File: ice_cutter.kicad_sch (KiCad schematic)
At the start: 156 parts, among them J1 Conn_01x01_Male, J2 Barrel_Jack, J3 pot, J4 Conn_01x01_Male, J5 program, J6 program2, J7 hands, J8 UART, J9 xt60, M1 Motor_Servo, M2 Motor_Servo, Q1 Q_PMOS_GSD, Q11 Q_NMOS_GSD, Q12 Q_NMOS_GSD, Q13 Q_NMOS_GSD, Q14 Q_NMOS_GSD, Q2 Q_PMOS_GSD, Q3 Q_PMOS_GSD, Q4 S8550, Q5 Q_NMOS_GSD, Q7 Q_NMOS_GSD, SW1 SW_Push, SW2 SW_Push, SW3 SW_Push, U1 LM317_TO-252, U10 TMP117, U11 TM1620, U12 INA219AxD, U2 LM317_TO-252, U3 INA219AxD, U4 LM317_TO-252, U5 INA219AxD, U6 FJ4301AH, U7 FJ4301AH, U8 STM32G030XX, U9 SHT30-DIS

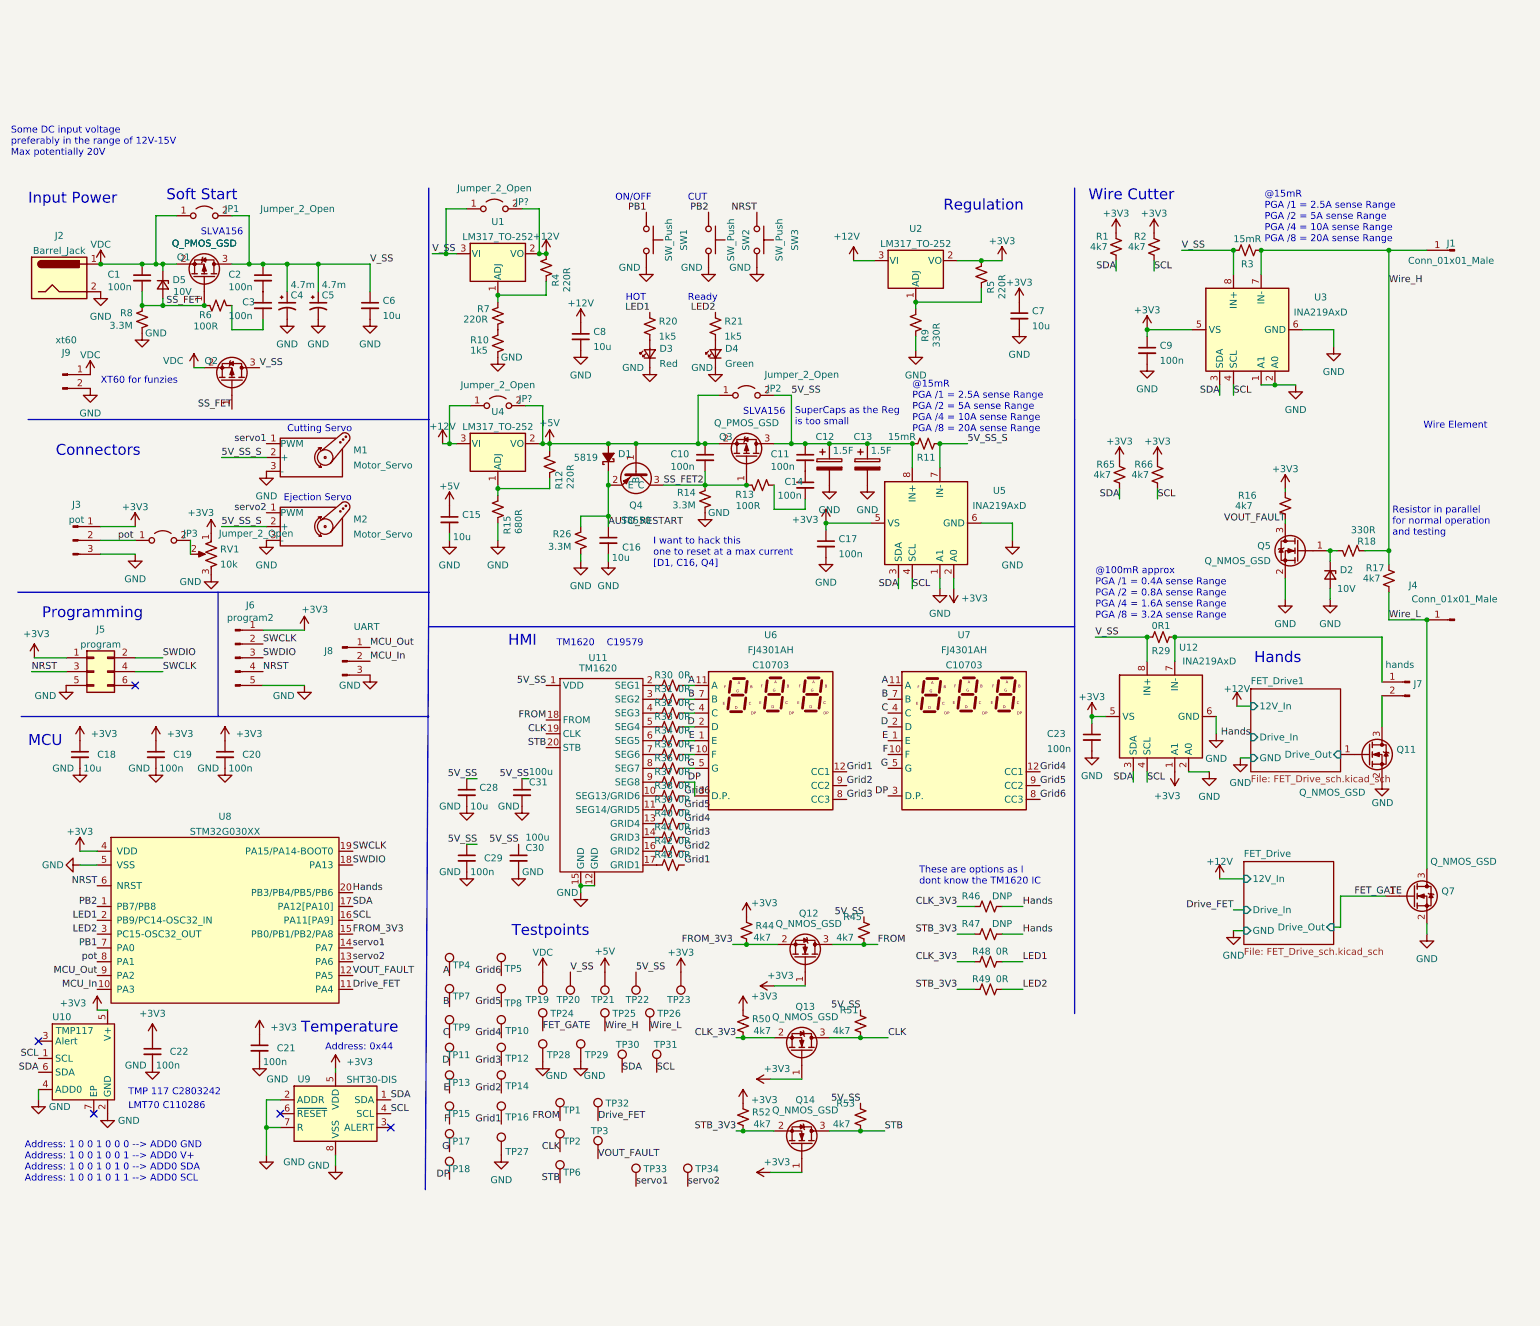
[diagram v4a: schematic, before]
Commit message: major schematic changes, 5V is now the highest voltage, added more FETs for Wire conduction, more for SS, opamp for current hack, removed Regs, XT60 and significantly changed wiring and R values for sections... Still a lot to be done, cant be solved now
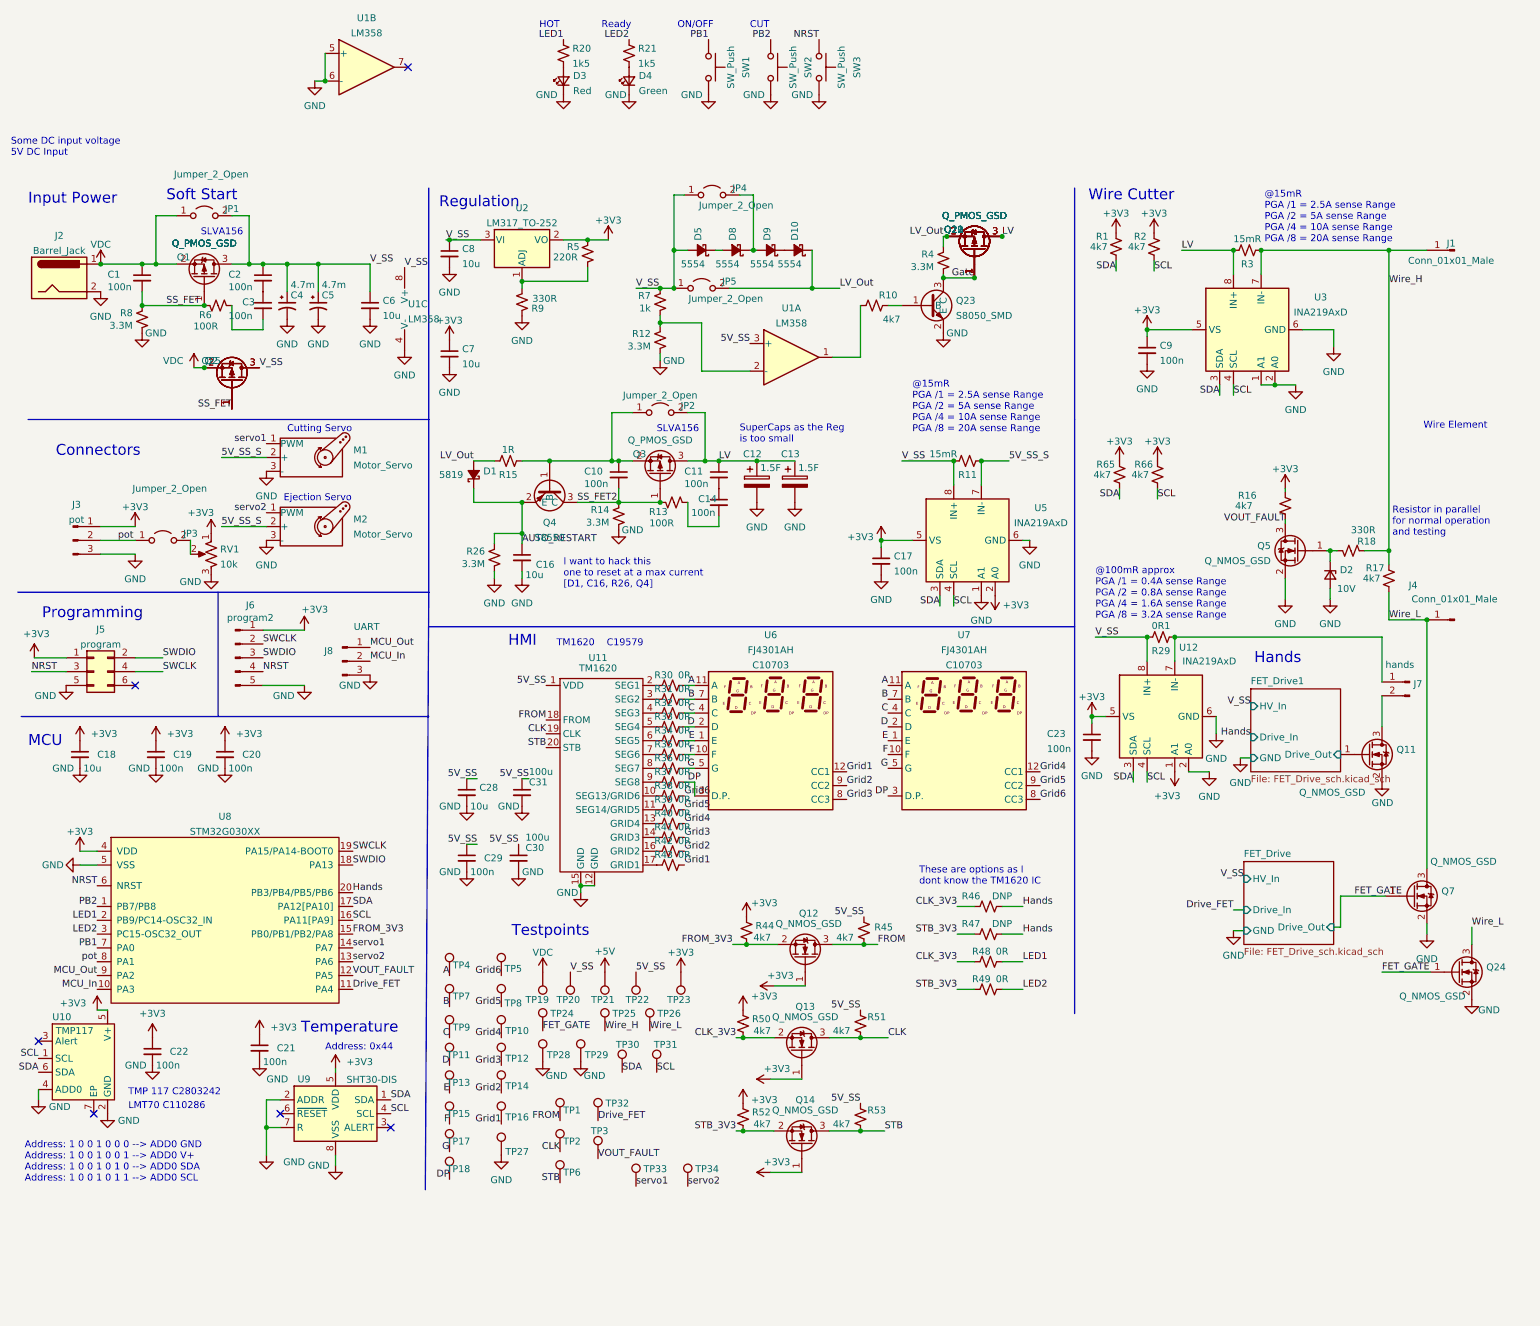
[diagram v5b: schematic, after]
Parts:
- removed C15: 10u, Capacitor_SMD:C_0603_1608Metric, symbol Device:C_Small
- removed D5: 10V, Diode_SMD:D_SOD-123, symbol Device:D_Zener_Small
- removed J9: xt60, UCT:XT60PW-M, symbol Connector:Conn_01x02_Male
- removed JP? (x2): Jumper_2_Open, Jumper:SolderJumper-2_P1.3mm_Open_RoundedPad1.0x1.5mm, symbol Jumper:Jumper_2_Open
- removed U1, U4: LM317_TO-252, Package_TO_SOT_SMD:TO-252-2, symbol Regulator_Linear:LM317_TO-252
- added D10, D5, D8, D9: 5554, Diode_SMD:D_SMA, symbol Device:D_Schottky_Small_Filled
- added JP4, JP5: Jumper_2_Open, Jumper:SolderJumper-2_P1.3mm_Open_RoundedPad1.0x1.5mm, symbol Jumper:Jumper_2_Open
- added Q19, Q20, Q21, Q22, Q25: Q_PMOS_GSD, Package_TO_SOT_SMD:SOT-23, symbol Device:Q_PMOS_GSD
- added Q23: S8050_SMD, Package_TO_SOT_SMD:SOT-23, symbol MyDevices:S8050_SMD
- added Q24: Q_NMOS_GSD, Package_TO_SOT_SMD:TO-252-2, symbol Device:Q_NMOS_GSD
- added U1: LM358, Package_SO:SOIC-8_3.9x4.9mm_P1.27mm, symbol Amplifier_Operational:LM358
- Q11, Q7: LCSC C130980 -> C709962
- R10: value 1k5 -> 4k7; LCSC C25867 -> C25900
- R12, R4: value 220R -> 3.3M; LCSC C25091 -> C25741
- R15: value 680R -> 1R; footprint Resistor_SMD:R_0402_1005Metric -> Resistor_SMD:R_2512_6332Metric; Extended 0 -> 1; LCSC C25130 -> C11254; Price 0.0007 -> 0.087
- R7: value 220R -> 1k; LCSC C25091 -> (none)
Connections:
- net +5V: no longer C10.1, D1.2 (A), JP2.1 (A), Q3.2 (S), Q4.1 (B), R12.2
- net 5V_SS: now also U1.3 (+); no longer C11.1, C12.1, C13.1, JP2.2 (B), Q3.3 (D), R11.1, U5.8 (IN+)
- net FET_GATE: now also Q24.1 (G)
- net GND: now also R12.2, Q23.2 (E), Q24.2 (S), U1.4 (V-), U1.5 (+), U1.6 (-); no longer R10.1, R15.1
- net SS_FET: now also Q25.1 (G)
- net VDC: now also Q25.2 (S)
- net V_SS: now also C8.1, R11.1, R7.1, U2.3 (VI), U5.8 (IN+), D5.2 (A), JP4.1 (A), JP5.1 (A), Q25.3 (D), U1.8 (V+); no longer R3.1, U3.8 (IN+)
- net Wire_L: now also Q24.3 (D)
- net at R7.2: now also R12.1, U1.2 (-); no longer R4.1
- net at R15.2: now also C10.1, JP2.1 (A), Q3.2 (S), Q4.1 (B); no longer R12.1
- net at R10.2: now also U1.1; no longer R7.1
- removed net +12V: C8.1, R4.2, U2.3 (VI)
- new net: D10.2 (A), D9.1 (K)
- new net: D8.1 (K), D9.2 (A), JP4.2 (B)
- new net: D5.1 (K), D8.2 (A)
- new net: Q23.1 (B), R10.1
- new net Gate: Q19.1 (G), Q20.1 (G), Q21.1 (G), Q22.1 (G), Q23.3 (C), R4.2
- new net LV: C11.1, C12.1, C13.1, JP2.2 (B), Q19.3 (D), Q20.3 (D), Q21.3 (D), Q22.3 (D), Q3.3 (D), R3.1, U3.8 (IN+)
- new net LV_Out: D1.2 (A), D10.1 (K), JP5.2 (B), Q19.2 (S), Q20.2 (S), Q21.2 (S), Q22.2 (S), R15.1, R4.1
- no-connect marks 5 -> 6
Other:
- sheet FET_Drive ports: added HV_In; removed 12V_In
- sheet FET_Drive1 ports: added HV_In; removed 12V_In
- note added: "I want to hack this one to reset at a max current [D1, C16, R26, Q4]"
- note added: "Some DC input voltage 5V DC Input"
- note removed: "I want to hack this one to reset at a max current [D1, C16, Q4]"
- note removed: "Some DC input voltage preferably in the range of 12V-15V Max potentially 20V"
- note removed: "XT60 for funzies"
- moved on the sheet: C10, C11, C12, C13, C14, C16, C17, C7, C8, D1, D3, D4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

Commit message: more mods, taking it to a solution. Mostly on layer 3 and power management
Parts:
- added C15: 100n, Capacitor_SMD:C_0402_1005Metric, symbol Device:C_Small
- R12: value 3.3M -> 4k7; LCSC C25741 -> C25900
- R7: value 1k -> 220R; LCSC (none) -> C25091
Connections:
- net 5V_SS: no longer C28.1, C29.1, C30.1, C31.1, R45.2, R51.2, R53.2, U11.1 (VDD)
- net GND: now also R12.1, C15.2; no longer R12.2
- net LV_Out: now also R7.2
- net V_SS: now also C28.1, C29.1, C30.1, C31.1, R45.2, R51.2, R53.2, U11.1 (VDD), C15.1; no longer R7.1
- new net: R12.2, R7.1, U1.2 (-)
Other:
- moved on the sheet: C28, C29, C30, C31, U1A

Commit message: potential new version. Still to do Silkscreen and resistor value confirmations
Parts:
- removed TP22: TestPoint, TestPoint:TestPoint_Pad_D2.0mm, symbol Connector:TestPoint
- added TP?: TestPoint, TestPoint:TestPoint_Pad_D2.0mm, symbol Connector:TestPoint
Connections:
- net 5V_SS is gone; now on net V_SS: U1.3 (+)
- net LV: now also TP?.1
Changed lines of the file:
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@@
     (effects (font (size 1.27 1.27)) (justify left bottom))
   )
+  (label "LV" (at 127 157.48 0)
+    (effects (font (size 1.27 1.27)) (justify left bottom))
+  )
   (label "MCU_In" (at 26.67 160.655 180)
     (effects (font (size 1.27 1.27)) (justify right bottom))
@@
     (effects (font (size 1.27 1.27)) (justify left bottom))
   )
+  (label "V_SS" (at 151.765 41.91 180)
+    (effects (font (size 1.27 1.27)) (justify right bottom))
+  )
   (label "NRST" (at 14.605 102.235 0)
     (effects (font (size 1.27 1.27)) (justify left bottom))
@@
     (effects (font (size 1.27 1.27)) (justify left bottom))
   )
-  (label "5V_SS" (at 125.73 157.48 0)
-    (effects (font (size 1.27 1.27)) (justify left bottom))
-  )
   (label "SWCLK" (at 73.66 135.255 0)
     (effects (font (size 1.27 1.27)) (justify left bottom))
@@
     (effects (font (size 1.27 1.27)) (justify left bottom))
   )
-  (label "5V_SS" (at 151.765 41.91 180)
-    (effects (font (size 1.27 1.27)) (justify right bottom))
-  )
   (label "Drive_FET" (at 73.66 160.655 0)
     (effects (font (size 1.27 1.27)) (justify left bottom))
@@
     (pin "1")
   )
-  (symbol (lib_id "Connector:TestPoint") (at 125.73 157.48 180) (unit 1)
-    (in_bom yes) (on_board yes)
-    (property "Reference" "TP22" (id 0) (at 123.825 162.56 0)
-      (effects (font (size 1.27 1.27)) (justify right))
-    )
-    (property "Value" "TestPoint" (id 1) (at 124.46 163.195 0)
-      (effects (font (size 1.27 1.27)) (justify right) hide)
-    )
-    (property "Footprint" "TestPoint:TestPoint_Pad_D2.0mm" (id 2) (at 120.65 157.48 0)
-      (effects (font (size 1.27 1.27)) hide)
-    )
-    (property "Datasheet" "~" (id 3) (at 120.65 157.48 0)
-      (effects (font (size 1.27 1.27)) hide)
-    )
-    (property "Populate" "No" (id 4) (at 125.73 157.48 0)
-      (effects (font (size 1.27 1.27)) hide)
-    )
-    (pin "1")
-  )
   (symbol (lib_id "Connector:Conn_01x03_Male") (at 22.225 78.105 0) (unit 1)
     (in_bom yes) (on_board yes) (fields_autoplaced)
@@
     (pin "3")
   )
+  (symbol (lib_id "Connector:TestPoint") (at 127 157.48 180) (unit 1)
+    (in_bom yes) (on_board yes)
+    (property "Reference" "TP?" (id 0) (at 124.46 162.56 0)
+      (effects (font (size 1.27 1.27)) (justify right))
+    )
+    (property "Value" "TestPoint" (id 1) (at 125.73 163.195 0)
+      (effects (font (size 1.27 1.27)) (justify right) hide)
+    )
+    (property "Footprint" "TestPoint:TestPoint_Pad_D2.0mm" (id 2) (at 121.92 157.48 0)
+      (effects (font (size 1.27 1.27)) hide)
+    )
+    (property "Datasheet" "~" (id 3) (at 121.92 157.48 0)
+      (effects (font (size 1.27 1.27)) hide)
+    )
+    (property "Populate" "No" (id 4) (at 127 157.48 0)
+      (effects (font (size 1.27 1.27)) hide)
+    )
+    (pin "1")
+  )
   (symbol (lib_id "power:GND") (at 36.83 174.625 0) (unit 1)
     (in_bom yes) (on_board yes)
@@
       (reference "TP21") (unit 1) (value "TestPoint") (footprint "TestPoint:TestPoint_Pad_D2.0mm")
     )
-    (path "/5cd2c641-9219-4ecf-8a99-e9ad548e97f6"
-      (reference "TP22") (unit 1) (value "TestPoint") (footprint "TestPoint:TestPoint_Pad_D2.0mm")
-    )
     (path "/ed0a645a-8744-4edf-9701-e8ea6d3c5ed9"
       (reference "TP23") (unit 1) (value "TestPoint") (footprint "TestPoint:TestPoint_Pad_D2.0mm")
@@
       (reference "TP34") (unit 1) (value "TestPoint") (footprint "TestPoint:TestPoint_Pad_D2.0mm")
     )
+    (path "/e99d92eb-91e5-4201-a2a4-2e283a85591e"
+      (reference "TP?") (unit 1) (value "TestPoint") (footprint "TestPoint:TestPoint_Pad_D2.0mm")
+    )
     (path "/967eb049-5189-4394-bd91-3e7a661ecab5"

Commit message: hadnt saved... this is the last commit message
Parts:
- gave numbers to parts that had none: 1
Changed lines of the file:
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@@
   (symbol (lib_id "Connector:TestPoint") (at 127 157.48 180) (unit 1)
     (in_bom yes) (on_board yes)
-    (property "Reference" "TP?" (id 0) (at 124.46 162.56 0)
+    (property "Reference" "TP22" (id 0) (at 124.46 162.56 0)
       (effects (font (size 1.27 1.27)) (justify right))
     )
@@
       (reference "TP21") (unit 1) (value "TestPoint") (footprint "TestPoint:TestPoint_Pad_D2.0mm")
     )
+    (path "/e99d92eb-91e5-4201-a2a4-2e283a85591e"
+      (reference "TP22") (unit 1) (value "TestPoint") (footprint "TestPoint:TestPoint_Pad_D2.0mm")
+    )
     (path "/ed0a645a-8744-4edf-9701-e8ea6d3c5ed9"
       (reference "TP23") (unit 1) (value "TestPoint") (footprint "TestPoint:TestPoint_Pad_D2.0mm")
@@
       (reference "TP34") (unit 1) (value "TestPoint") (footprint "TestPoint:TestPoint_Pad_D2.0mm")
     )
-    (path "/e99d92eb-91e5-4201-a2a4-2e283a85591e"
-      (reference "TP?") (unit 1) (value "TestPoint") (footprint "TestPoint:TestPoint_Pad_D2.0mm")
-    )
     (path "/967eb049-5189-4394-bd91-3e7a661ecab5"
